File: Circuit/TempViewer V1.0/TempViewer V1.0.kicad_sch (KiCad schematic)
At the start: 1 part, among them U1 LTC2451xDDB

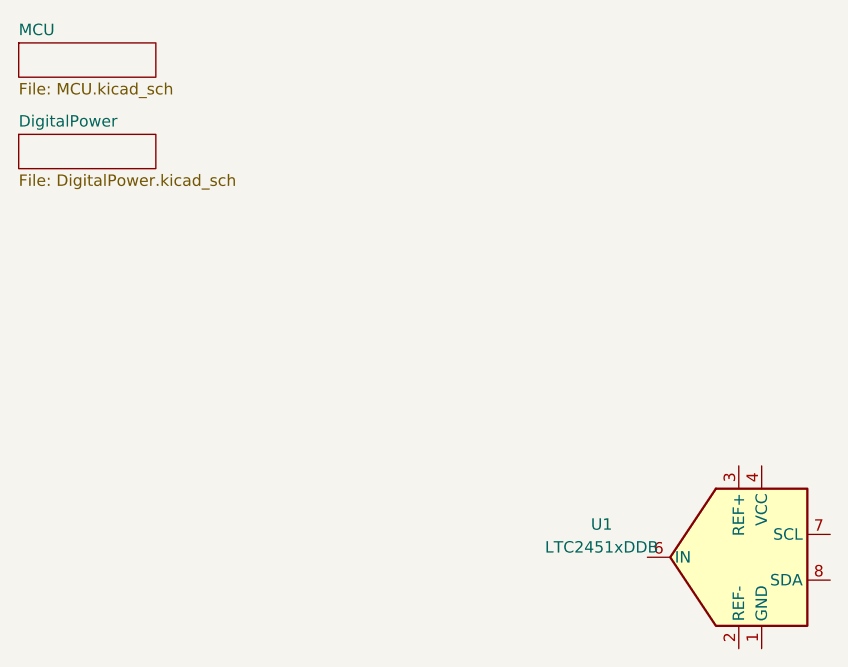
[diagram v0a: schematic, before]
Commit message: Analog Circuits added
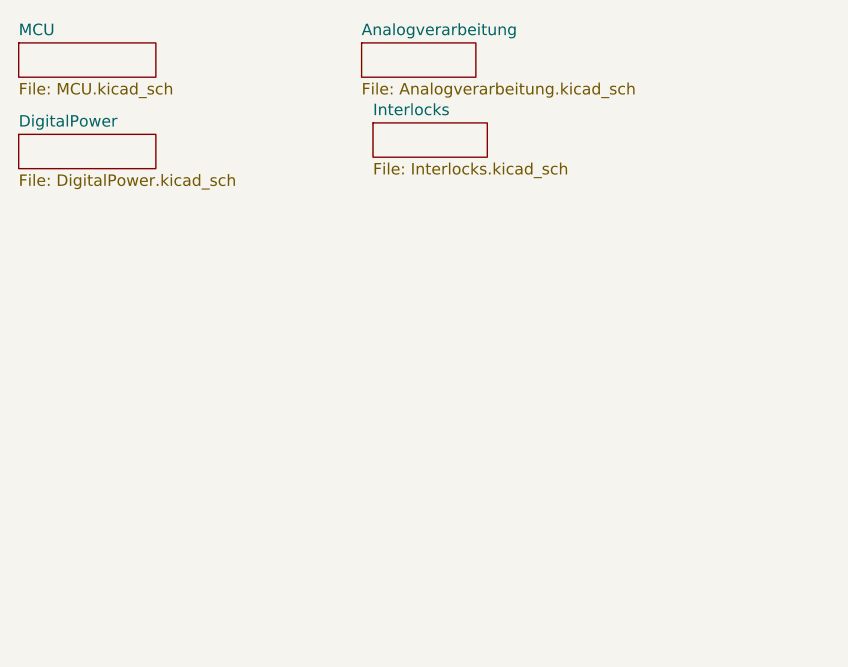
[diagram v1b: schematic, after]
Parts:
- removed U1: LTC2451xDDB, Package_DFN_QFN:DFN-8-1EP_2x3mm_P0.5mm_EP0.56x2.15mm, symbol Analog_ADC:LTC2451xDDB
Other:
- added sheet Analogverarbeitung (Analogverarbeitung.kicad_sch)
- added sheet Interlocks (Interlocks.kicad_sch)
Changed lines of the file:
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@@
 (kicad_sch (version 20230121) (generator eeschema)
   (paper "A4")
-  (symbol (lib_id "Analog_ADC:LTC2451xDDB") (at 100.33 74.93 0) (unit 1)
-    (in_bom yes) (on_board yes) (dnp no) (fields_autoplaced)
-    (property "Reference" "U1" (at 85.09 71.2821 0)
-      (effects (font (size 1.27 1.27)))
+  (sheet (at 58.42 17.78) (size 12.7 3.81) (fields_autoplaced)
+    (stroke (width 0.1524) (type solid))
+    (fill (color 0 0 0 0.0000))
+    (property "Sheetname" "Analogverarbeitung" (at 58.42 17.0684 0)
+      (effects (font (size 1.27 1.27)) (justify left bottom))
     )
-    (property "Value" "LTC2451xDDB" (at 85.09 73.8221 0)
-      (effects (font (size 1.27 1.27)))
+    (property "Sheetfile" "Analogverarbeitung.kicad_sch" (at 58.42 22.1746 0)
+      (effects (font (size 1.27 1.27)) (justify left top))
     )
-    (property "Footprint" "Package_DFN_QFN:DFN-8-1EP_2x3mm_P0.5mm_EP0.56x2.15mm" (at 85.09 62.23 0)
-      (effects (font (size 1.27 1.27)) hide)
-    )
-    (property "Datasheet" "https://www.analog.com/media/en/technical-documentation/data-sheets/2451fg.pdf" (at 82.55 62.23 0)
-      (effects (font (size 1.27 1.27)) hide)
-    )
-    (pin "7")
-    (pin "2")
-    (pin "5")
-    (pin "9")
-    (pin "1")
-    (pin "4")
-    (pin "3")
-    (pin "6")
-    (pin "8")
     (instances
       (project "TempViewer V1.0"
-        (path "/9be733a6-d9bf-4549-8c43-ef6367cdf2b9"
-          (reference "U1") (unit 1)
-        )
+        (path "/9be733a6-d9bf-4549-8c43-ef6367cdf2b9" (page "4"))
       )
     )
+  )
+  (sheet (at 59.69 26.67) (size 12.7 3.81) (fields_autoplaced)
+    (stroke (width 0.1524) (type solid))
+    (fill (color 0 0 0 0.0000))
+    (property "Sheetname" "Interlocks" (at 59.69 25.9584 0)
+      (effects (font (size 1.27 1.27)) (justify left bottom))
+    )
+    (property "Sheetfile" "Interlocks.kicad_sch" (at 59.69 31.0646 0)
+      (effects (font (size 1.27 1.27)) (justify left top))
+    )
+    (instances
+      (project "TempViewer V1.0"
+        (path "/9be733a6-d9bf-4549-8c43-ef6367cdf2b9" (page "5"))
+      )
+    )
